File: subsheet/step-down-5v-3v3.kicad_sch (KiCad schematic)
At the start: 7 parts, among them U1001 TLV62569DBV

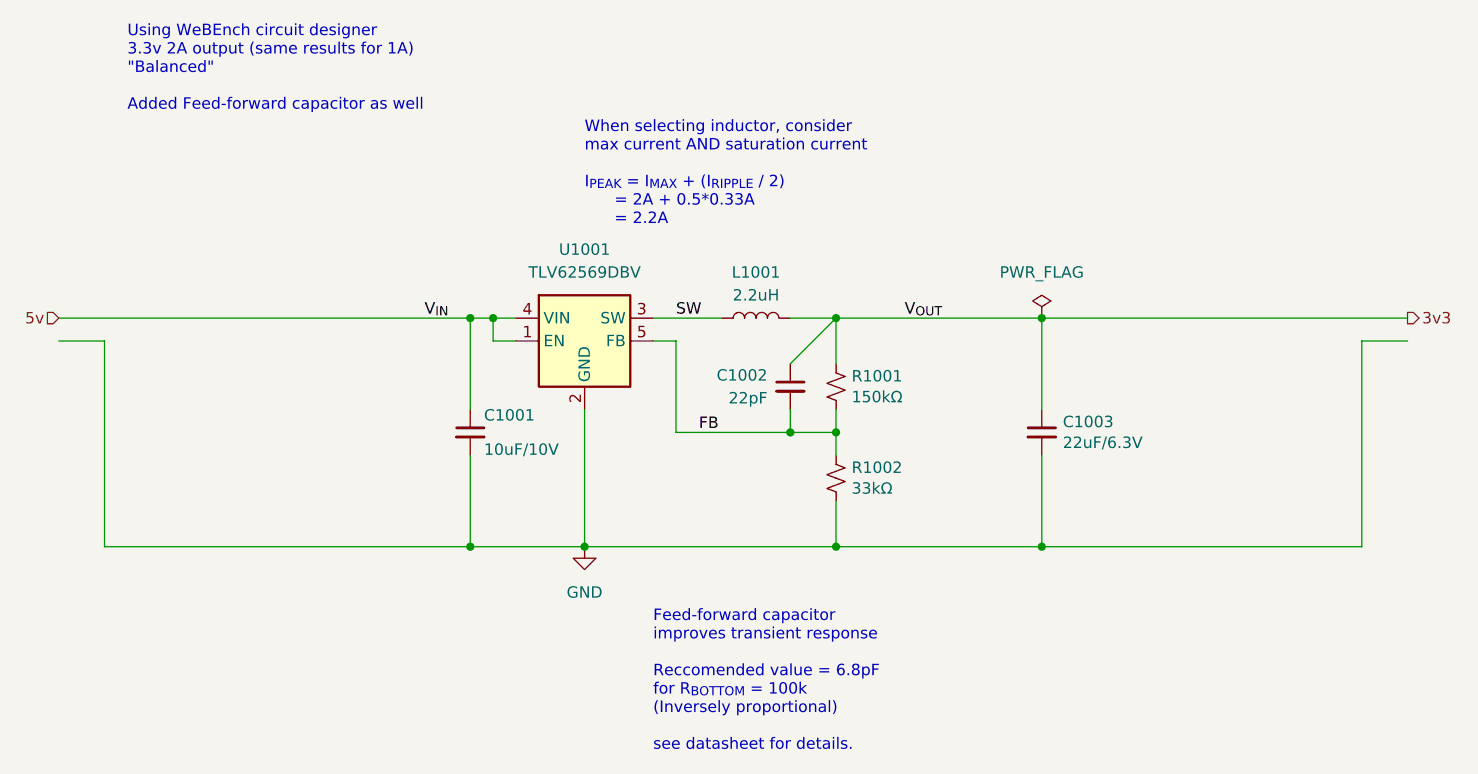
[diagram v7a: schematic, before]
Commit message: Move all subsheets into 'main' subsheet, below root
Keeping all the subsheets in a dedicated 'subsheet' folder makes things
much, much neater. However, specifying filepaths for subsheets has an
interesting problem; they use paths RELATIVE TO THE PARENT SHEET.

The consequence of is that if a subsheet is part of the root sheet, it
needs to be prefixed with 'subsheet/', but NOT if it's further down.
This inconsistency can be resolved by having a single 'main' sheet at
the top that doesn't move.

It's also useful to have a top-level space to put down changelogs,
descriptions etc.
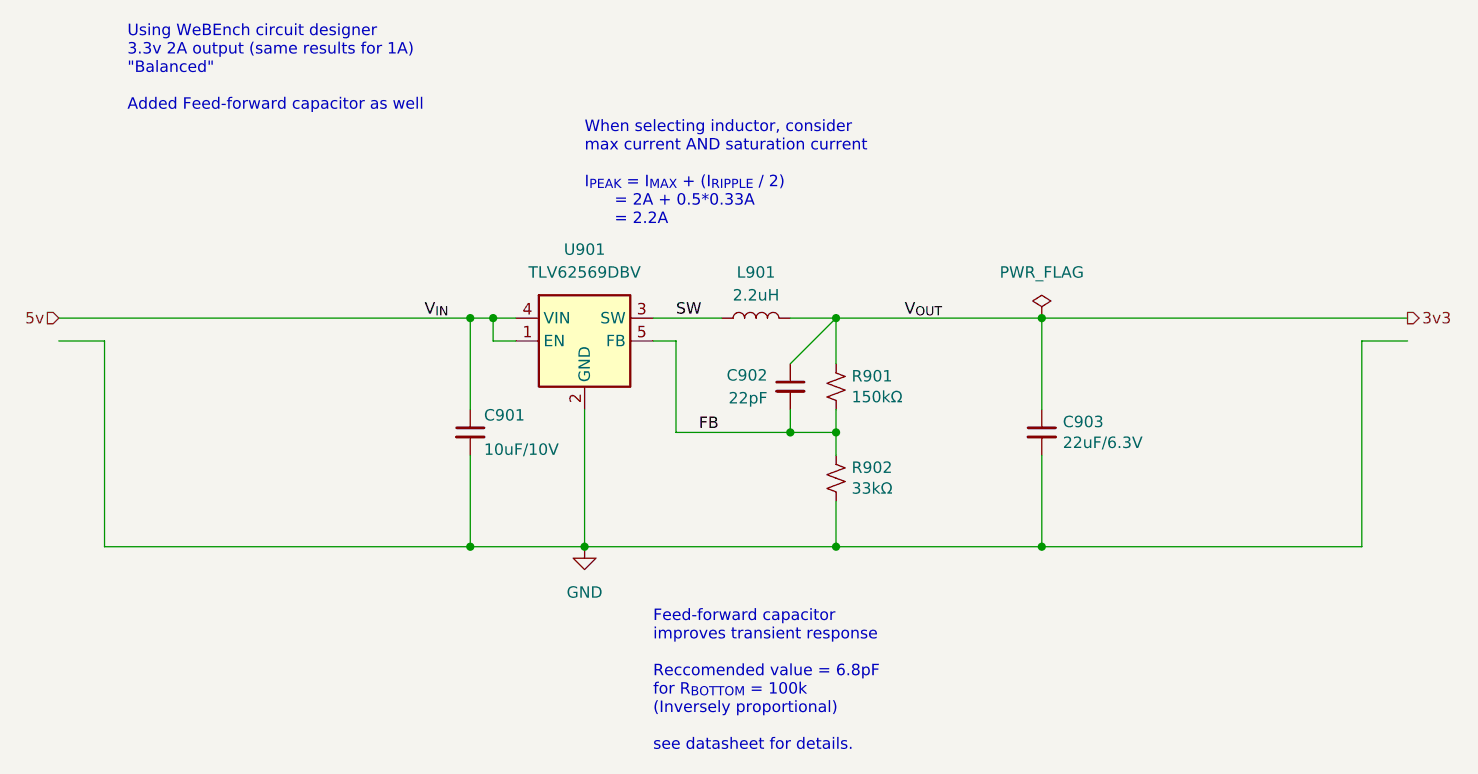
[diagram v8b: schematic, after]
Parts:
- renumbered C1001 to C901, C1002 to C902, C1003 to C903, L1001 to L901, R1001 to R901, R1002 to R902, U1001 to U901
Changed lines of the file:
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@@
 	(label "SW"
 		(at 93.98 50.8 0)
-		(fields_autoplaced yes)
 		(effects
 			(font
@@
 	(label "V_{OUT}"
 		(at 119.38 50.8 0)
-		(fields_autoplaced yes)
 		(effects
 			(font
@@
 	(label "V_{IN}"
 		(at 66.04 50.8 0)
-		(fields_autoplaced yes)
 		(effects
 			(font
@@
 	(label "FB"
 		(at 96.52 63.5 0)
-		(fields_autoplaced yes)
 		(effects
 			(font
@@
 		(shape output)
 		(at 175.26 50.8 0)
-		(fields_autoplaced yes)
 		(effects
 			(font
@@
 		(shape input)
 		(at 25.4 50.8 180)
-		(fields_autoplaced yes)
 		(effects
 			(font
@@
 		(on_board yes)
 		(dnp no)
-		(property "Reference" "C1003"
+		(property "Reference" "C903"
 			(at 136.9568 62.3316 0)
 			(effects
@@
 		(instances
 			(project "ESP_bare_chip_test_board"
-				(path "/45b6f84a-e69b-48be-a49b-bc68872e2c15/28425a28-8968-4679-b18b-58814452f93f/cab84238-ee51-476d-8b41-60559ed008d0"
-					(reference "C1003")
-					(unit 1)
-				)
-			)
-			(project "puzzle-shield-ESP32"
-				(path "/7f264da7-ad23-4f41-956f-57553b2e7107/5a6cdf82-c956-4eb3-893f-6bfd5dd30cf7/4bb5c589-ebbf-42a1-af33-7c273c73680b"
-					(reference "C1803")
-					(unit 1)
-				)
-				(path "/7f264da7-ad23-4f41-956f-57553b2e7107/5a6cdf82-c956-4eb3-893f-6bfd5dd30cf7/1067c906-482e-4c74-a717-42efa4aea55f"
-					(reference "C1703")
+				(path "/45b6f84a-e69b-48be-a49b-bc68872e2c15/f48098a1-cacc-4192-b650-2a34a2ba76dc/1ca534e3-2263-4539-8aa0-ff724a69b5d8/cab84238-ee51-476d-8b41-60559ed008d0"
+					(reference "C903")
 					(unit 1)
 				)
@@
 		(dnp no)
 		(fields_autoplaced yes)
-		(property "Reference" "L1001"
+		(property "Reference" "L901"
 			(at 102.87 45.72 90)
 			(effects
@@
 		(instances
 			(project "ESP_bare_chip_test_board"
-				(path "/45b6f84a-e69b-48be-a49b-bc68872e2c15/28425a28-8968-4679-b18b-58814452f93f/cab84238-ee51-476d-8b41-60559ed008d0"
-					(reference "L1001")
-					(unit 1)
-				)
-			)
-			(project "puzzle-shield-ESP32"
-				(path "/7f264da7-ad23-4f41-956f-57553b2e7107/5a6cdf82-c956-4eb3-893f-6bfd5dd30cf7/4bb5c589-ebbf-42a1-af33-7c273c73680b"
-					(reference "L1801")
-					(unit 1)
-				)
-				(path "/7f264da7-ad23-4f41-956f-57553b2e7107/5a6cdf82-c956-4eb3-893f-6bfd5dd30cf7/1067c906-482e-4c74-a717-42efa4aea55f"
-					(reference "L1701")
+				(path "/45b6f84a-e69b-48be-a49b-bc68872e2c15/f48098a1-cacc-4192-b650-2a34a2ba76dc/1ca534e3-2263-4539-8aa0-ff724a69b5d8/cab84238-ee51-476d-8b41-60559ed008d0"
+					(reference "L901")
 					(unit 1)
 				)
@@
 		(dnp no)
 		(fields_autoplaced yes)
-		(property "Reference" "C1002"
+		(property "Reference" "C902"
 			(at 104.14 57.1563 0)
 			(effects
@@
 		(instances
 			(project "ESP_bare_chip_test_board"
-				(path "/45b6f84a-e69b-48be-a49b-bc68872e2c15/28425a28-8968-4679-b18b-58814452f93f/cab84238-ee51-476d-8b41-60559ed008d0"
-					(reference "C1002")
-					(unit 1)
-				)
-			)
-			(project "puzzle-shield-ESP32"
-				(path "/7f264da7-ad23-4f41-956f-57553b2e7107/5a6cdf82-c956-4eb3-893f-6bfd5dd30cf7/4bb5c589-ebbf-42a1-af33-7c273c73680b"
-					(reference "C1802")
-					(unit 1)
-				)
-				(path "/7f264da7-ad23-4f41-956f-57553b2e7107/5a6cdf82-c956-4eb3-893f-6bfd5dd30cf7/1067c906-482e-4c74-a717-42efa4aea55f"
-					(reference "C1702")
+				(path "/45b6f84a-e69b-48be-a49b-bc68872e2c15/f48098a1-cacc-4192-b650-2a34a2ba76dc/1ca534e3-2263-4539-8aa0-ff724a69b5d8/cab84238-ee51-476d-8b41-60559ed008d0"
+					(reference "C902")
 					(unit 1)
 				)
@@
 		(on_board yes)
 		(dnp no)
-		(property "Reference" "R1001"
+		(property "Reference" "R901"
 			(at 113.4872 57.2516 0)
 			(effects
@@
 		(instances
 			(project "ESP_bare_chip_test_board"
-				(path "/45b6f84a-e69b-48be-a49b-bc68872e2c15/28425a28-8968-4679-b18b-58814452f93f/cab84238-ee51-476d-8b41-60559ed008d0"
-					(reference "R1001")
-					(unit 1)
-				)
-			)
-			(project "puzzle-shield-ESP32"
-				(path "/7f264da7-ad23-4f41-956f-57553b2e7107/5a6cdf82-c956-4eb3-893f-6bfd5dd30cf7/1067c906-482e-4c74-a717-42efa4aea55f"
-					(reference "R1701")
-					(unit 1)
-				)
-				(path "/7f264da7-ad23-4f41-956f-57553b2e7107/5a6cdf82-c956-4eb3-893f-6bfd5dd30cf7/4bb5c589-ebbf-42a1-af33-7c273c73680b"
-					(reference "R1801")
+				(path "/45b6f84a-e69b-48be-a49b-bc68872e2c15/f48098a1-cacc-4192-b650-2a34a2ba76dc/1ca534e3-2263-4539-8aa0-ff724a69b5d8/cab84238-ee51-476d-8b41-60559ed008d0"
+					(reference "R901")
 					(unit 1)
 				)
@@
 		(dnp no)
 		(fields_autoplaced yes)
-		(property "Reference" "U1001"
+		(property "Reference" "U901"
 			(at 83.82 43.18 0)
 			(effects
@@
 		(instances
 			(project "ESP_bare_chip_test_board"
-				(path "/45b6f84a-e69b-48be-a49b-bc68872e2c15/28425a28-8968-4679-b18b-58814452f93f/cab84238-ee51-476d-8b41-60559ed008d0"
-					(reference "U1001")
-					(unit 1)
-				)
-			)
-			(project "puzzle-shield-ESP32"
-				(path "/7f264da7-ad23-4f41-956f-57553b2e7107/5a6cdf82-c956-4eb3-893f-6bfd5dd30cf7/4bb5c589-ebbf-42a1-af33-7c273c73680b"
-					(reference "U1801")
-					(unit 1)
-				)
-				(path "/7f264da7-ad23-4f41-956f-57553b2e7107/5a6cdf82-c956-4eb3-893f-6bfd5dd30cf7/1067c906-482e-4c74-a717-42efa4aea55f"
-					(reference "U1701")
+				(path "/45b6f84a-e69b-48be-a49b-bc68872e2c15/f48098a1-cacc-4192-b650-2a34a2ba76dc/1ca534e3-2263-4539-8aa0-ff724a69b5d8/cab84238-ee51-476d-8b41-60559ed008d0"
+					(reference "U901")
 					(unit 1)
 				)
@@
 		(dnp no)
 		(fields_autoplaced yes)
-		(property "Reference" "#FLG01001"
+		(property "Reference" "#FLG901"
 			(at 134.62 48.895 0)
 			(effects
@@
 		(instances
 			(project "ESP_bare_chip_test_board"
-				(path "/45b6f84a-e69b-48be-a49b-bc68872e2c15/28425a28-8968-4679-b18b-58814452f93f/cab84238-ee51-476d-8b41-60559ed008d0"
-					(reference "#FLG01001")
-					(unit 1)
-				)
-			)
-			(project "puzzle-shield-ESP32"
-				(path "/7f264da7-ad23-4f41-956f-57553b2e7107/5a6cdf82-c956-4eb3-893f-6bfd5dd30cf7/1067c906-482e-4c74-a717-42efa4aea55f"
-					(reference "#FLG01701")
-					(unit 1)
-				)
-				(path "/7f264da7-ad23-4f41-956f-57553b2e7107/5a6cdf82-c956-4eb3-893f-6bfd5dd30cf7/4bb5c589-ebbf-42a1-af33-7c273c73680b"
-					(reference "#FLG01801")
+				(path "/45b6f84a-e69b-48be-a49b-bc68872e2c15/f48098a1-cacc-4192-b650-2a34a2ba76dc/1ca534e3-2263-4539-8aa0-ff724a69b5d8/cab84238-ee51-476d-8b41-60559ed008d0"
+					(reference "#FLG901")
 					(unit 1)
 				)
@@
 		(dnp no)
 		(fields_autoplaced yes)
-		(property "Reference" "#PWR01001"
+		(property "Reference" "#PWR901"
 			(at 83.82 82.55 0)
 			(effects
@@
 		(instances
 			(project "ESP_bare_chip_test_board"
-				(path "/45b6f84a-e69b-48be-a49b-bc68872e2c15/28425a28-8968-4679-b18b-58814452f93f/cab84238-ee51-476d-8b41-60559ed008d0"
-					(reference "#PWR01001")
-					(unit 1)
-				)
-			)
-			(project "puzzle-shield-ESP32"
-				(path "/7f264da7-ad23-4f41-956f-57553b2e7107/5a6cdf82-c956-4eb3-893f-6bfd5dd30cf7/4bb5c589-ebbf-42a1-af33-7c273c73680b"
-					(reference "#PWR01801")
-					(unit 1)
-				)
-				(path "/7f264da7-ad23-4f41-956f-57553b2e7107/5a6cdf82-c956-4eb3-893f-6bfd5dd30cf7/1067c906-482e-4c74-a717-42efa4aea55f"
-					(reference "#PWR01701")
+				(path "/45b6f84a-e69b-48be-a49b-bc68872e2c15/f48098a1-cacc-4192-b650-2a34a2ba76dc/1ca534e3-2263-4539-8aa0-ff724a69b5d8/cab84238-ee51-476d-8b41-60559ed008d0"
+					(reference "#PWR901")
 					(unit 1)
 				)
@@
 		(on_board yes)
 		(dnp no)
-		(property "Reference" "R1002"
+		(property "Reference" "R902"
 			(at 113.4872 67.4116 0)
 			(effects
@@
 		(instances
 			(project "ESP_bare_chip_test_board"
-				(path "/45b6f84a-e69b-48be-a49b-bc68872e2c15/28425a28-8968-4679-b18b-58814452f93f/cab84238-ee51-476d-8b41-60559ed008d0"
-					(reference "R1002")
-					(unit 1)
-				)
-			)
-			(project "puzzle-shield-ESP32"
-				(path "/7f264da7-ad23-4f41-956f-57553b2e7107/5a6cdf82-c956-4eb3-893f-6bfd5dd30cf7/1067c906-482e-4c74-a717-42efa4aea55f"
-					(reference "R1702")
-					(unit 1)
-				)
-				(path "/7f264da7-ad23-4f41-956f-57553b2e7107/5a6cdf82-c956-4eb3-893f-6bfd5dd30cf7/4bb5c589-ebbf-42a1-af33-7c273c73680b"
-					(reference "R1802")
+				(path "/45b6f84a-e69b-48be-a49b-bc68872e2c15/f48098a1-cacc-4192-b650-2a34a2ba76dc/1ca534e3-2263-4539-8aa0-ff724a69b5d8/cab84238-ee51-476d-8b41-60559ed008d0"
+					(reference "R902")
 					(unit 1)
 				)
@@
 		(on_board yes)
 		(dnp no)
-		(property "Reference" "C1001"
+		(property "Reference" "C901"
 			(at 72.644 61.595 0)
 			(effects
@@
 		(instances
 			(project "ESP_bare_chip_test_board"
-				(path "/45b6f84a-e69b-48be-a49b-bc68872e2c15/28425a28-8968-4679-b18b-58814452f93f/cab84238-ee51-476d-8b41-60559ed008d0"
-					(reference "C1001")
-					(unit 1)
-				)
-			)
-			(project "puzzle-shield-ESP32"
-				(path "/7f264da7-ad23-4f41-956f-57553b2e7107/5a6cdf82-c956-4eb3-893f-6bfd5dd30cf7/4bb5c589-ebbf-42a1-af33-7c273c73680b"
-					(reference "C1801")
-					(unit 1)
-				)
-				(path "/7f264da7-ad23-4f41-956f-57553b2e7107/5a6cdf82-c956-4eb3-893f-6bfd5dd30cf7/1067c906-482e-4c74-a717-42efa4aea55f"
-					(reference "C1701")
-					(unit 1)
-				)
+				(path "/45b6f84a-e69b-48be-a49b-bc68872e2c15/f48098a1-cacc-4192-b650-2a34a2ba76dc/1ca534e3-2263-4539-8aa0-ff724a69b5d8/cab84238-ee51-476d-8b41-60559ed008d0"
+					(reference "C901")
+					(unit 1)
+				)
